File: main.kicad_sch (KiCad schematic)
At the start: 3 parts, among them J101 Conn_02x12_Odd_Even

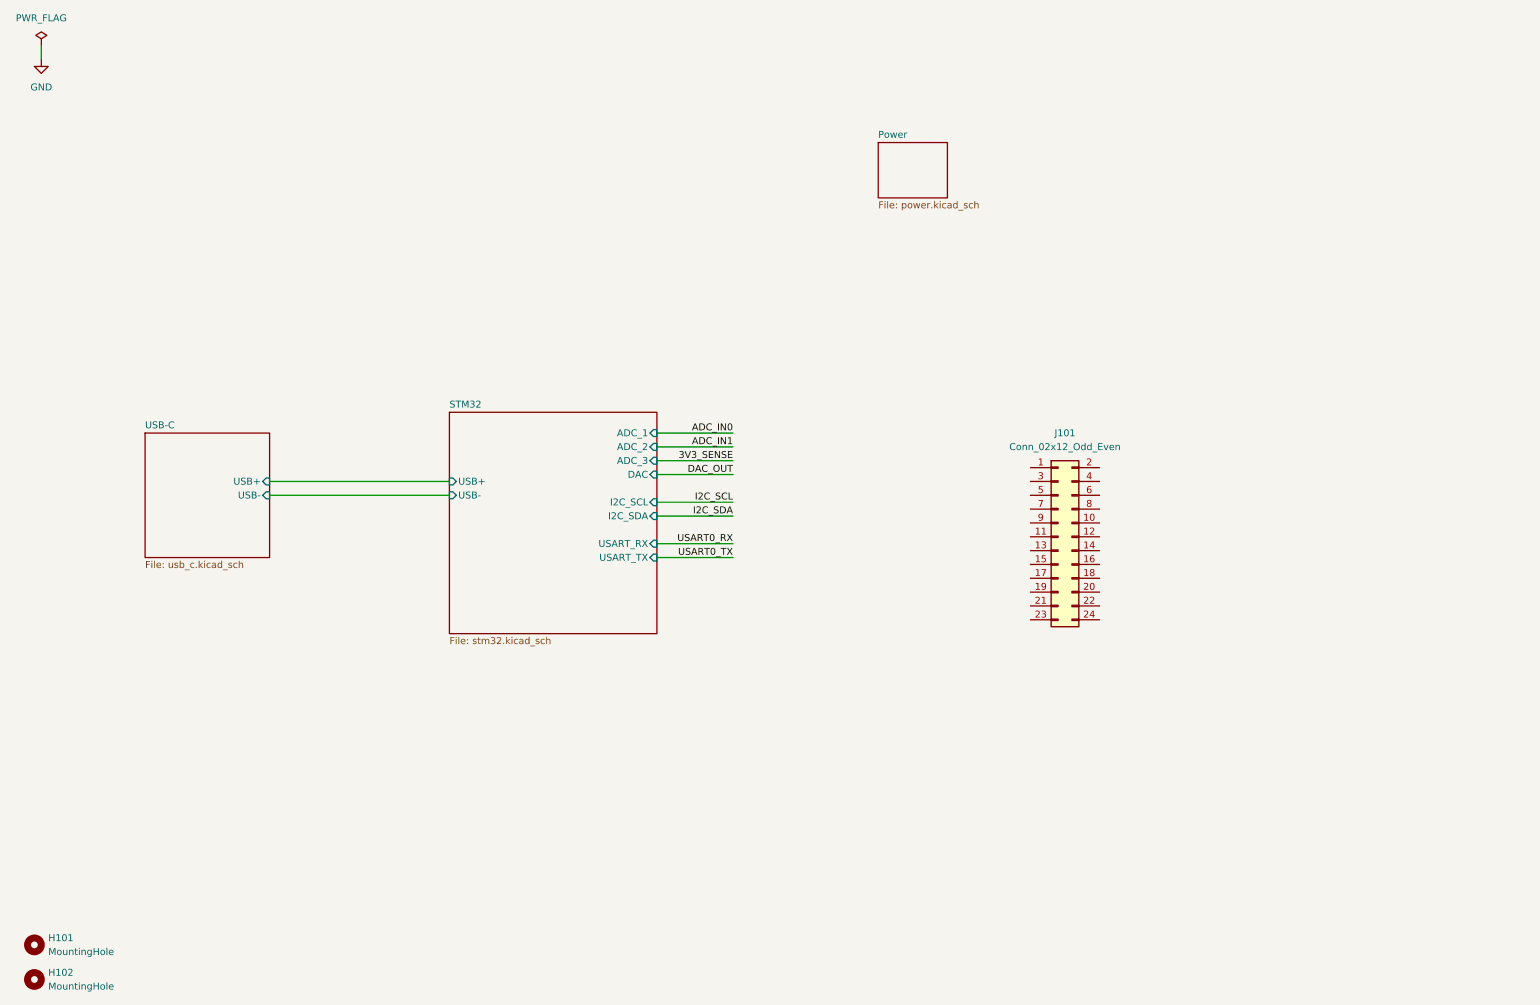
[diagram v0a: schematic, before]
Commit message: add basic structure, update readme
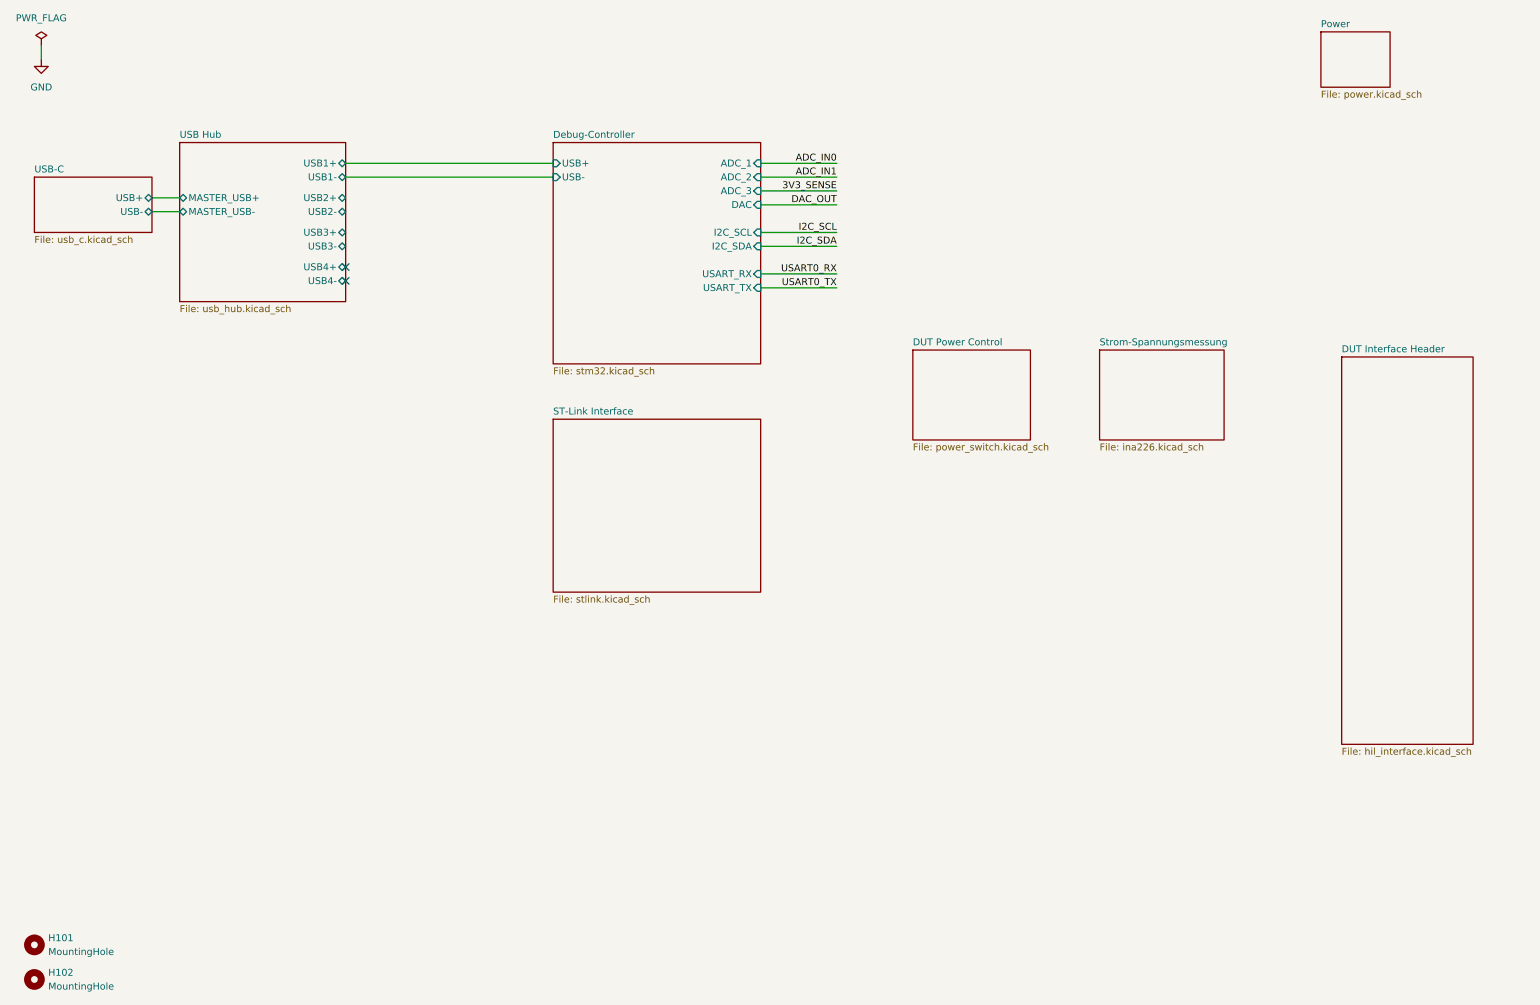
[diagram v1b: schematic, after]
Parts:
- removed J101: Conn_02x12_Odd_Even, Connector_PinHeader_1.27mm:PinHeader_2x12_P1.27mm_Horizontal, symbol Connector_Generic:Conn_02x12_Odd_Even
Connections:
- no-connect marks 0 -> 2
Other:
- sheet STM32 renamed Debug-Controller
- added sheet DUT Interface Header (hil_interface.kicad_sch)
- added sheet DUT Power Control (power_switch.kicad_sch)
- added sheet ST-Link Interface (stlink.kicad_sch)
- added sheet Strom-Spannungsmessung (ina226.kicad_sch)
- added sheet USB Hub (usb_hub.kicad_sch)

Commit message: Update schematic for DebugBoard with connector and power symbols.
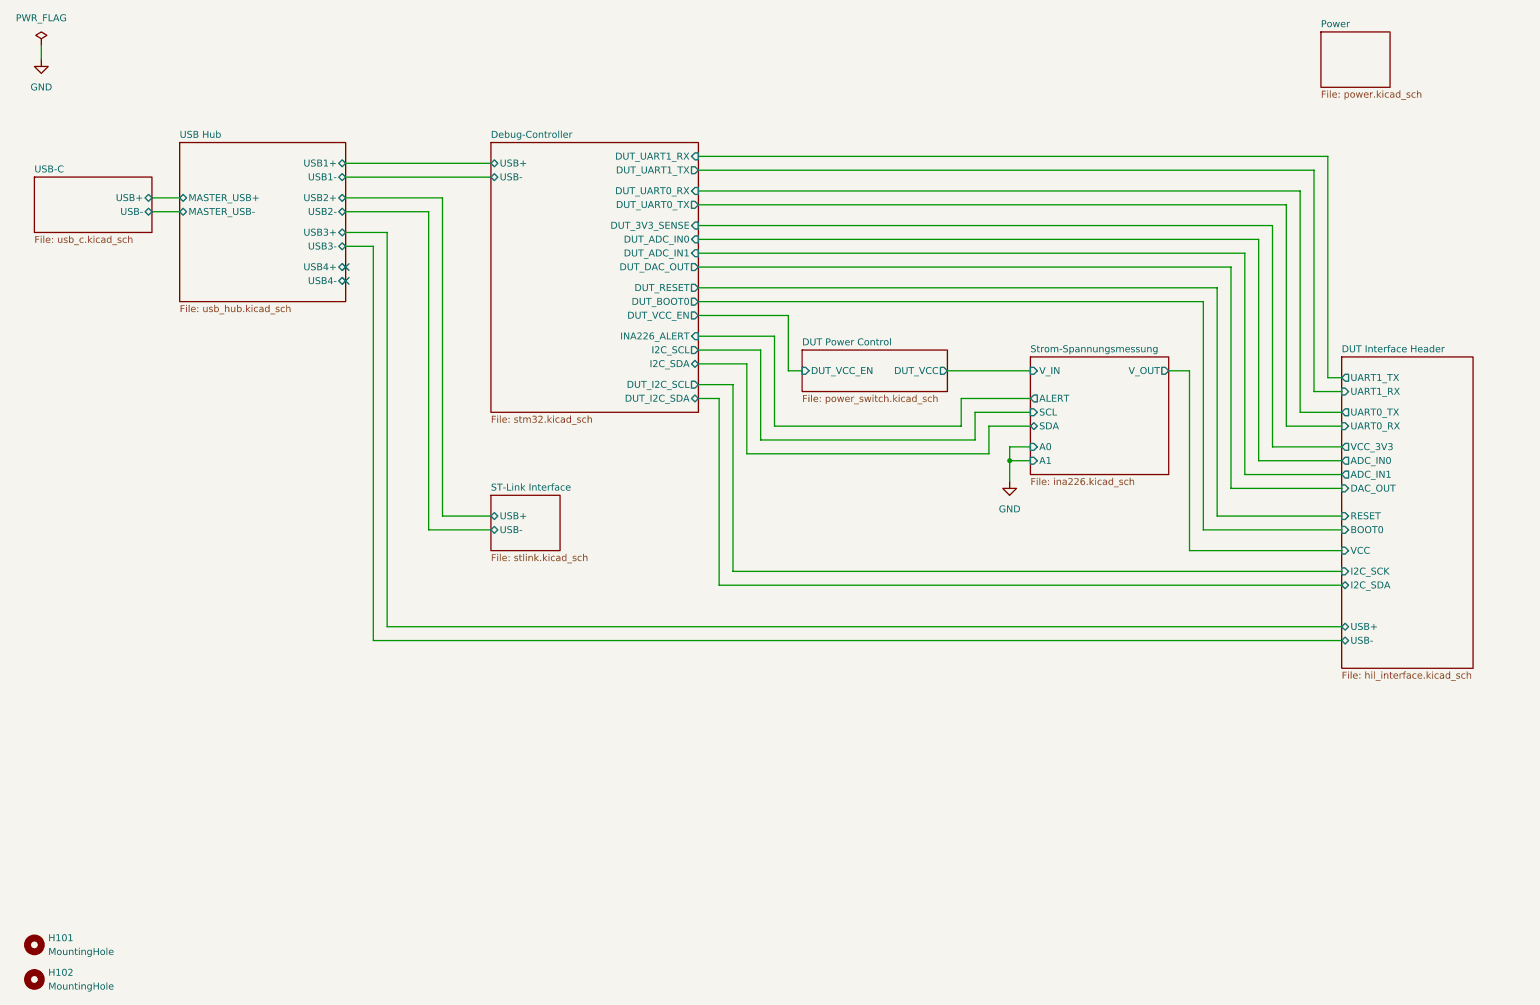
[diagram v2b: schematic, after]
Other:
- sheet DUT Interface Header ports: added ADC_IN0, ADC_IN1, BOOT0, DAC_OUT, I2C_SCK, I2C_SDA, RESET, UART0_RX, UART0_TX, UART1_RX, UART1_TX, USB+, USB-, VCC, VCC_3V3; removed none
- sheet DUT Power Control ports: added DUT_VCC, DUT_VCC_EN; removed none
- sheet Debug-Controller ports: added DUT_3V3_SENSE, DUT_ADC_IN0, DUT_ADC_IN1, DUT_BOOT0, DUT_DAC_OUT, DUT_I2C_SCL, DUT_I2C_SDA, DUT_RESET, DUT_UART0_RX, DUT_UART0_TX, DUT_UART1_RX, DUT_UART1_TX, DUT_VCC_EN, INA226_ALERT; removed ADC_1, ADC_2, ADC_3, DAC, USART_RX, USART_TX
- sheet ST-Link Interface ports: added USB+, USB-; removed none
- sheet Strom-Spannungsmessung ports: added A0, A1, ALERT, SCL, SDA, V_IN, V_OUT; removed none

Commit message: Update USB-C and USB-Hub Schematics with New Titles and Reference Changes
- Changed title from "DebugBoard" to "USB-C" in usb_c.kicad_sch.
- Changed title from "DebugBoard" to "USB-Hub" in usb_hub.kicad_sch.
- Updated multiple component references in usb_c.kicad_sch to new identifiers (#PWR0301 to #PWR0312, D301, U301, etc.).
- Updated component reference from "R103" to "R501" in usb_hub.kicad_sch.
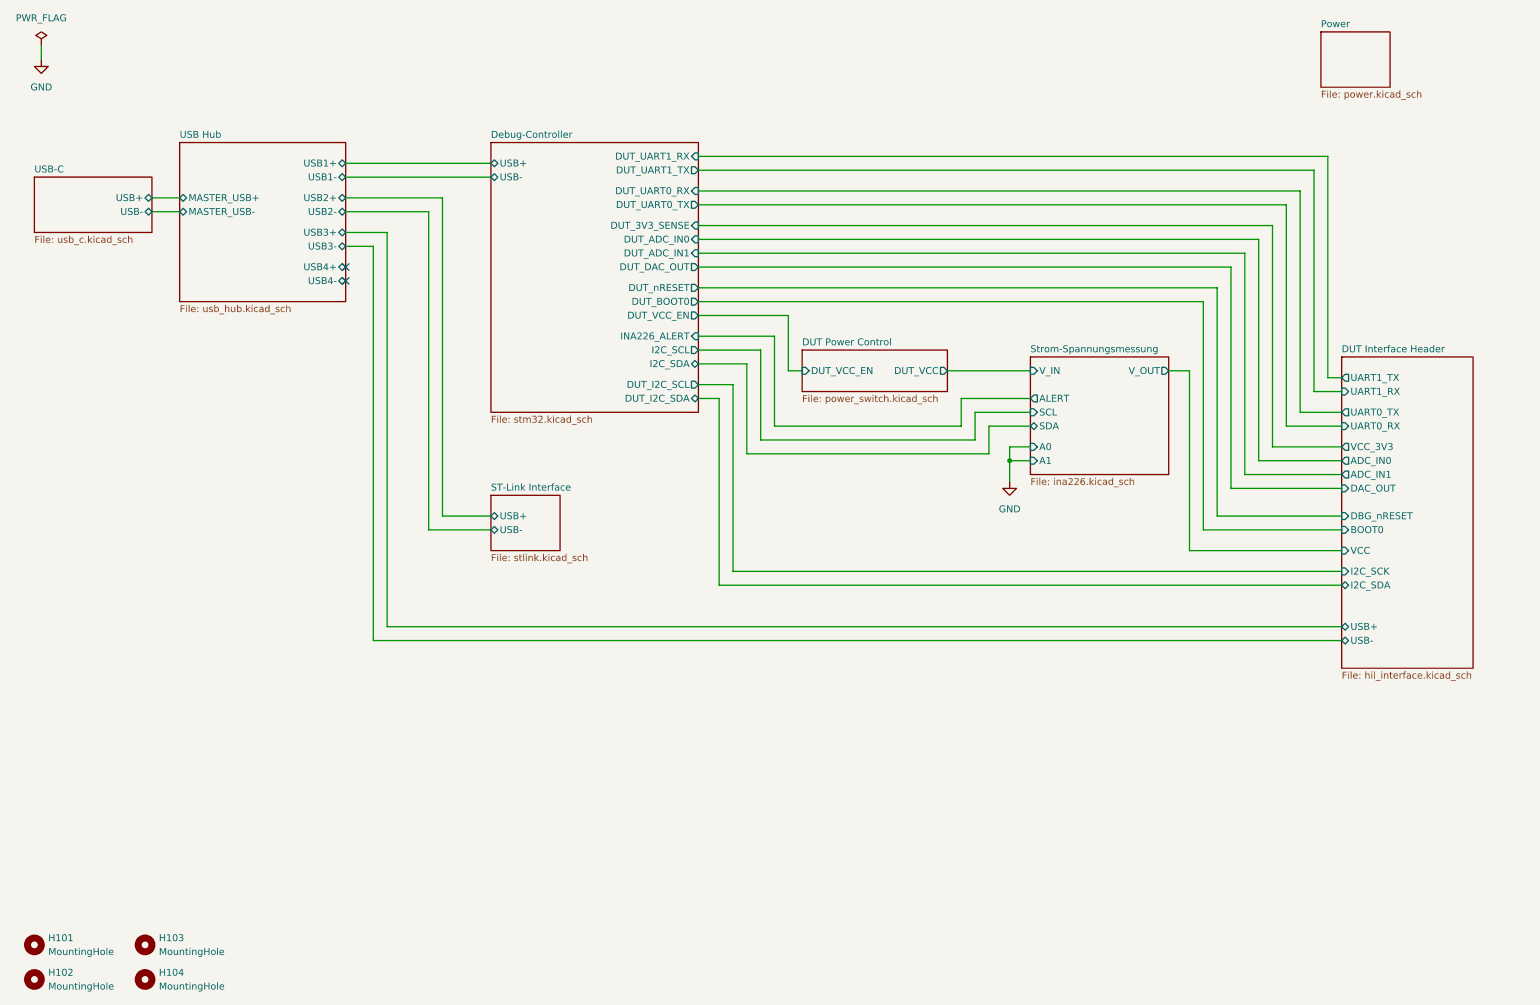
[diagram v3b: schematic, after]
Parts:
- added H103, H104: MountingHole, MountingHole:MountingHole_3.2mm_M3, symbol Mechanical:MountingHole
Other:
- sheet DUT Interface Header ports: added DBG_nRESET; removed RESET
- sheet Debug-Controller ports: added DUT_nRESET; removed DUT_RESET
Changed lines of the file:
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@@
 		(dnp no)
 		(fields_autoplaced yes)
-		(property "Reference" "#PWR0102"
+		(property "Reference" "#PWR0101"
 			(at 19.05 29.21 0)
 			(effects
@@
 			(project "main"
 				(path "/f228839c-6576-40b2-ae70-679b7b460639"
-					(reference "#PWR0102")
+					(reference "#PWR0101")
 					(unit 1)
 				)
@@
 		(dnp no)
 		(fields_autoplaced yes)
-		(property "Reference" "#PWR0101"
+		(property "Reference" "#PWR0102"
 			(at 196.85 106.68 0)
 			(effects
@@
 			(project "main"
 				(path "/f228839c-6576-40b2-ae70-679b7b460639"
-					(reference "#PWR0101")
+					(reference "#PWR0102")
+					(unit 1)
+				)
+			)
+		)
+	)
+	(symbol
+		(lib_id "Mechanical:MountingHole")
+		(at 38.1 191.77 0)
+		(unit 1)
+		(exclude_from_sim yes)
+		(in_bom no)
+		(on_board yes)
+		(dnp no)
+		(fields_autoplaced yes)
+		(property "Reference" "H104"
+			(at 40.64 190.4999 0)
+			(effects
+				(font
+					(size 1.27 1.27)
+				)
+				(justify left)
+			)
+		)
+		(property "Value" "MountingHole"
+			(at 40.64 193.0399 0)
+			(effects
+				(font
+					(size 1.27 1.27)
+				)
+				(justify left)
+			)
+		)
+		(property "Footprint" "MountingHole:MountingHole_3.2mm_M3"
+			(at 38.1 191.77 0)
+			(effects
+				(font
+					(size 1.27 1.27)
+				)
+				(hide yes)
+			)
+		)
+		(property "Datasheet" "~"
+			(at 38.1 191.77 0)
+			(effects
+				(font
+					(size 1.27 1.27)
+				)
+				(hide yes)
+			)
+		)
+		(property "Description" "Mounting Hole without connection"
+			(at 38.1 191.77 0)
+			(effects
+				(font
+					(size 1.27 1.27)
+				)
+				(hide yes)
+			)
+		)
+		(property "LCSC" ""
+			(at 38.1 191.77 0)
+			(effects
+				(font
+					(size 1.27 1.27)
+				)
+				(hide yes)
+			)
+		)
+		(property "MOUSER" ""
+			(at 38.1 191.77 0)
+			(effects
+				(font
+					(size 1.27 1.27)
+				)
+			)
+		)
+		(instances
+			(project "main"
+				(path "/f228839c-6576-40b2-ae70-679b7b460639"
+					(reference "H104")
+					(unit 1)
+				)
+			)
+		)
+	)
+	(symbol
+		(lib_id "Mechanical:MountingHole")
+		(at 38.1 185.42 0)
+		(unit 1)
+		(exclude_from_sim yes)
+		(in_bom no)
+		(on_board yes)
+		(dnp no)
+		(fields_autoplaced yes)
+		(property "Reference" "H103"
+			(at 40.64 184.1499 0)
+			(effects
+				(font
+					(size 1.27 1.27)
+				)
+				(justify left)
+			)
+		)
+		(property "Value" "MountingHole"
+			(at 40.64 186.6899 0)
+			(effects
+				(font
+					(size 1.27 1.27)
+				)
+				(justify left)
+			)
+		)
+		(property "Footprint" "MountingHole:MountingHole_3.2mm_M3"
+			(at 38.1 185.42 0)
+			(effects
+				(font
+					(size 1.27 1.27)
+				)
+				(hide yes)
+			)
+		)
+		(property "Datasheet" "~"
+			(at 38.1 185.42 0)
+			(effects
+				(font
+					(size 1.27 1.27)
+				)
+				(hide yes)
+			)
+		)
+		(property "Description" "Mounting Hole without connection"
+			(at 38.1 185.42 0)
+			(effects
+				(font
+					(size 1.27 1.27)
+				)
+				(hide yes)
+			)
+		)
+		(property "LCSC" ""
+			(at 38.1 185.42 0)
+			(effects
+				(font
+					(size 1.27 1.27)
+				)
+				(hide yes)
+			)
+		)
+		(property "MOUSER" ""
+			(at 38.1 185.42 0)
+			(effects
+				(font
+					(size 1.27 1.27)
+				)
+			)
+		)
+		(instances
+			(project "main"
+				(path "/f228839c-6576-40b2-ae70-679b7b460639"
+					(reference "H103")
 					(unit 1)
 				)
@@
 			)
 		)
-		(pin "DUT_RESET" output
+		(pin "DUT_nRESET" output
 			(at 139.7 64.77 0)
 			(effects
@@
 			)
 		)
-		(pin "RESET" input
+		(pin "DBG_nRESET" input
 			(at 257.81 106.68 180)
 			(effects
